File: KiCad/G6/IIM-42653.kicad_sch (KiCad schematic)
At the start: 8 parts, among them U13 IIM-42653, U14 IIM-42653

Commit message: uhhhh im confused gang
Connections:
- net AP-SDI renamed AP-SDI-IIM1
- net AP-SDI-IIM1: no longer U14.14 (AP_SDA/AP_SDIO/AP_SDI)
- net AP-SDO renamed AP-SDO-IIM1
- net AP-SDO-IIM1: no longer U14.1 (AP_SDO/AP_AD0)
- net SPI-SDO-MAIN renamed SPI-SDO-IIM1
- net SPI-SDO-IIM1: no longer U14.11 (AUX1_SDO)
- new net AP-SDI-IIM2: U14.14 (AP_SDA/AP_SDIO/AP_SDI)
- new net AP-SDO-IIM2: U14.1 (AP_SDO/AP_AD0)
- new net SPI-SDO-IIM2: U14.11 (AUX1_SDO)
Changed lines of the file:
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@@
 		)
 	)
-	(global_label "AP-SDI"
+	(global_label "AP-SDI-IIM1"
 		(shape input)
 		(at 44.45 92.71 180)
@@
 		)
 		(property "Intersheetrefs" "${INTERSHEET_REFS}"
-			(at 34.4495 92.71 0)
+			(at 29.0066 92.71 0)
 			(effects
 				(font
@@
 		)
 	)
-	(global_label "AP-SDO"
+	(global_label "AP-SDO-IIM1"
 		(shape input)
 		(at 44.45 95.25 180)
@@
 		)
 		(property "Intersheetrefs" "${INTERSHEET_REFS}"
-			(at 33.7238 95.25 0)
+			(at 28.2809 95.25 0)
 			(effects
 				(font
@@
 		)
 	)
-	(global_label "SPI-SDO-MAIN"
+	(global_label "SPI-SDO-IIM1"
 		(shape input)
 		(at 44.45 107.95 180)
@@
 		)
 		(property "Intersheetrefs" "${INTERSHEET_REFS}"
-			(at 26.9504 107.95 0)
+			(at 27.5552 107.95 0)
 			(effects
 				(font
@@
 		)
 	)
-	(global_label "AP-SDI"
+	(global_label "AP-SDI-IIM2"
 		(shape input)
 		(at 180.34 100.33 180)
@@
 		)
 		(property "Intersheetrefs" "${INTERSHEET_REFS}"
-			(at 170.3395 100.33 0)
+			(at 164.8966 100.33 0)
 			(effects
 				(font
@@
 		)
 	)
-	(global_label "AP-SDO"
+	(global_label "AP-SDO-IIM2"
 		(shape input)
 		(at 180.34 102.87 180)
@@
 		)
 		(property "Intersheetrefs" "${INTERSHEET_REFS}"
-			(at 169.6138 102.87 0)
-			(effects
-				(font
-					(size 1.27 1.27)
-				)
-				(justify right)
-				(hide yes)
-			)
-		)
-	)
-	(global_label "SPI-SDO-MAIN"
+			(at 164.1709 102.87 0)
+			(effects
+				(font
+					(size 1.27 1.27)
+				)
+				(justify right)
+				(hide yes)
+			)
+		)
+	)
+	(global_label "SPI-SDO-IIM2"
 		(shape input)
 		(at 180.34 115.57 180)
@@
 		)
 		(property "Intersheetrefs" "${INTERSHEET_REFS}"
-			(at 162.8404 115.57 0)
-			(effects
-				(font
+			(at 163.4452 115.57 0)
+			(effects
+				(font

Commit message: I think the schematics done uhhh idrk
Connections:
- net AP-CS-IIM1 is gone; now on net CS-IIM1: U13.12 (AP_CS)
- net AP-CS-IIM2 is gone; now on net CS-IIM2: U14.12 (AP_CS)
- net CS-IIM1: no longer U13.10 (AUX1_CS)
- net CS-IIM2: no longer U14.10 (AUX1_CS)
- net AP-SCLK renamed SCK-MAIN
- net AP-SDI-IIM1 renamed MOSI-IIM1
- net AP-SDI-IIM2 renamed MOSI-IIM2
- net AP-SDO-IIM1 renamed MISO-IIM1
- net AP-SDO-IIM2 renamed MISO-IIM2
- net INT1-IIM1-43: no longer names the net of U13.4 (INT1/INT)
- net INT1-IIM2-43: no longer names the net of U14.4 (INT1/INT)
- net INT2-IIM1-43: no longer names the net of U13.9 (INT2/FSYNC/CLKIN)
- net INT2-IIM2-43: no longer names the net of U14.9 (INT2/FSYNC/CLKIN)
- net SPI-SCK-MAIN: no longer names the net of U13.3 (AUX1_SCLK)
- net SPI-SCK-MAIN: no longer U14.3 (AUX1_SCLK)
- net SPI-SDO-IIM1: no longer names the net of U13.11 (AUX1_SDO)
- net SPI-SDO-IIM2: no longer names the net of U14.11 (AUX1_SDO)

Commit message: im sorry parsa :/
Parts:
- U13, U14: footprint IIM-42653:PQFN50P250X300X97-14N -> CC0603KRXQRQBB104:IIM42563
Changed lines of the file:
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@@
 			)
 		)
-		(property "Footprint" "IIM-42653:PQFN50P250X300X97-14N"
+		(property "Footprint" "CC0603KRXQRQBB104:IIM42563"
 			(at 72.39 100.33 0)
 			(effects
@@
 			)
 		)
-		(property "Footprint" "IIM-42653:PQFN50P250X300X97-14N"
+		(property "Footprint" "CC0603KRXQRQBB104:IIM42563"
 			(at 208.28 107.95 0)
 			(effects

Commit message: sasha sneaky academic
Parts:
- renumbered C8 to C10, C9 to C11, C10 to C12, C11 to C13, C6 to C8, C7 to C9, U13 to U10, U14 to U11
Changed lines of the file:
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@@
 		(dnp no)
 		(fields_autoplaced yes)
-		(property "Reference" "C8"
+		(property "Reference" "C10"
 			(at 121.92 86.3599 0)
 			(effects
@@
 			(project ""
 				(path "/99017594-210d-4d15-87a7-3152ef0d7b7c/5c9dde29-c732-426e-b6f2-0733aa54ee5a"
-					(reference "C8")
+					(reference "C10")
 					(unit 1)
 				)
@@
 		(dnp no)
 		(fields_autoplaced yes)
-		(property "Reference" "C6"
+		(property "Reference" "C8"
 			(at 110.49 74.9299 0)
 			(effects
@@
 			(project "G6"
 				(path "/99017594-210d-4d15-87a7-3152ef0d7b7c/5c9dde29-c732-426e-b6f2-0733aa54ee5a"
-					(reference "C6")
+					(reference "C8")
 					(unit 1)
 				)
@@
 		(dnp no)
 		(fields_autoplaced yes)
-		(property "Reference" "#PWR049"
+		(property "Reference" "#PWR042"
 			(at 106.68 66.04 0)
 			(effects
@@
 			(project ""
 				(path "/99017594-210d-4d15-87a7-3152ef0d7b7c/5c9dde29-c732-426e-b6f2-0733aa54ee5a"
-					(reference "#PWR049")
+					(reference "#PWR042")
 					(unit 1)
 				)
@@
 		(dnp no)
 		(fields_autoplaced yes)
-		(property "Reference" "#PWR035"
+		(property "Reference" "#PWR041"
 			(at 102.87 130.81 0)
 			(effects
@@
 			(project ""
 				(path "/99017594-210d-4d15-87a7-3152ef0d7b7c/5c9dde29-c732-426e-b6f2-0733aa54ee5a"
-					(reference "#PWR035")
+					(reference "#PWR041")
 					(unit 1)
 				)
@@
 		(dnp no)
 		(fields_autoplaced yes)
-		(property "Reference" "C10"
+		(property "Reference" "C12"
 			(at 246.38 93.9799 0)
 			(effects
@@
 			(project "G6"
 				(path "/99017594-210d-4d15-87a7-3152ef0d7b7c/5c9dde29-c732-426e-b6f2-0733aa54ee5a"
-					(reference "C10")
+					(reference "C12")
 					(unit 1)
 				)
@@
 		(dnp no)
 		(fields_autoplaced yes)
-		(property "Reference" "C7"
+		(property "Reference" "C9"
 			(at 110.49 86.3599 0)
 			(effects
@@
 			(project "G6"
 				(path "/99017594-210d-4d15-87a7-3152ef0d7b7c/5c9dde29-c732-426e-b6f2-0733aa54ee5a"
-					(reference "C7")
+					(reference "C9")
 					(unit 1)
 				)
@@
 		(dnp no)
 		(fields_autoplaced yes)
-		(property "Reference" "#PWR065"
+		(property "Reference" "#PWR048"
 			(at 254 106.68 0)
 			(effects
@@
 			(project "G6"
 				(path "/99017594-210d-4d15-87a7-3152ef0d7b7c/5c9dde29-c732-426e-b6f2-0733aa54ee5a"
-					(reference "#PWR065")
+					(reference "#PWR048")
 					(unit 1)
 				)
@@
 		(dnp no)
 		(fields_autoplaced yes)
-		(property "Reference" "C9"
+		(property "Reference" "C11"
 			(at 246.38 82.5499 0)
 			(effects
@@
 			(project "G6"
 				(path "/99017594-210d-4d15-87a7-3152ef0d7b7c/5c9dde29-c732-426e-b6f2-0733aa54ee5a"
-					(reference "C9")
+					(reference "C11")
 					(unit 1)
 				)
@@
 		(dnp no)
 		(fields_autoplaced yes)
-		(property "Reference" "U13"
+		(property "Reference" "U10"
 			(at 72.39 72.39 0)
 			(effects
@@
 			(project ""
 				(path "/99017594-210d-4d15-87a7-3152ef0d7b7c/5c9dde29-c732-426e-b6f2-0733aa54ee5a"
-					(reference "U13")
+					(reference "U10")
 					(unit 1)
 				)
@@
 		(dnp no)
 		(fields_autoplaced yes)
-		(property "Reference" "C11"
+		(property "Reference" "C13"
 			(at 257.81 93.9799 0)
 			(effects
@@
 			(project "G6"
 				(path "/99017594-210d-4d15-87a7-3152ef0d7b7c/5c9dde29-c732-426e-b6f2-0733aa54ee5a"
-					(reference "C11")
+					(reference "C13")
 					(unit 1)
 				)
@@
 		(dnp no)
 		(fields_autoplaced yes)
-		(property "Reference" "#PWR061"
+		(property "Reference" "#PWR044"
 			(at 118.11 99.06 0)
 			(effects
@@
 			(project ""
 				(path "/99017594-210d-4d15-87a7-3152ef0d7b7c/5c9dde29-c732-426e-b6f2-0733aa54ee5a"
-					(reference "#PWR061")
+					(reference "#PWR044")
 					(unit 1)
 				)
@@
 		(dnp no)
 		(fields_autoplaced yes)
-		(property "Reference" "#PWR064"
+		(property "Reference" "#PWR047"
 			(at 242.57 105.41 0)
 			(effects
@@
 			(project "G6"
 				(path "/99017594-210d-4d15-87a7-3152ef0d7b7c/5c9dde29-c732-426e-b6f2-0733aa54ee5a"
-					(reference "#PWR064")
+					(reference "#PWR047")
 					(unit 1)
 				)
@@
 		(dnp no)
 		(fields_autoplaced yes)
-		(property "Reference" "#PWR063"
+		(property "Reference" "#PWR046"
 			(at 242.57 73.66 0)
 			(effects
@@
 			(project "G6"
 				(path "/99017594-210d-4d15-87a7-3152ef0d7b7c/5c9dde29-c732-426e-b6f2-0733aa54ee5a"
-					(reference "#PWR063")
+					(reference "#PWR046")
 					(unit 1)
 				)
@@
 		(dnp no)
 		(fields_autoplaced yes)
-		(property "Reference" "#PWR060"
+		(property "Reference" "#PWR043"
 			(at 106.68 97.79 0)
 			(effects
@@
 			(project ""
 				(path "/99017594-210d-4d15-87a7-3152ef0d7b7c/5c9dde29-c732-426e-b6f2-0733aa54ee5a"
-					(reference "#PWR060")
+					(reference "#PWR043")
 					(unit 1)
 				)
@@
 		(dnp no)
 		(fields_autoplaced yes)
-		(property "Reference" "U14"
+		(property "Reference" "U11"
 			(at 208.28 80.01 0)
 			(effects
@@
 			(project "G6"
 				(path "/99017594-210d-4d15-87a7-3152ef0d7b7c/5c9dde29-c732-426e-b6f2-0733aa54ee5a"
-					(reference "U14")
+					(reference "U11")
 					(unit 1)
 				)
@@
 		(dnp no)
 		(fields_autoplaced yes)
-		(property "Reference" "#PWR062"
+		(property "Reference" "#PWR045"
 			(at 238.76 138.43 0)
 			(effects
@@
 			(project "G6"
 				(path "/99017594-210d-4d15-87a7-3152ef0d7b7c/5c9dde29-c732-426e-b6f2-0733aa54ee5a"
-					(reference "#PWR062")
-					(unit 1)
-				)
+					(reference "#PWR045")
+					(unit 1)
+				)

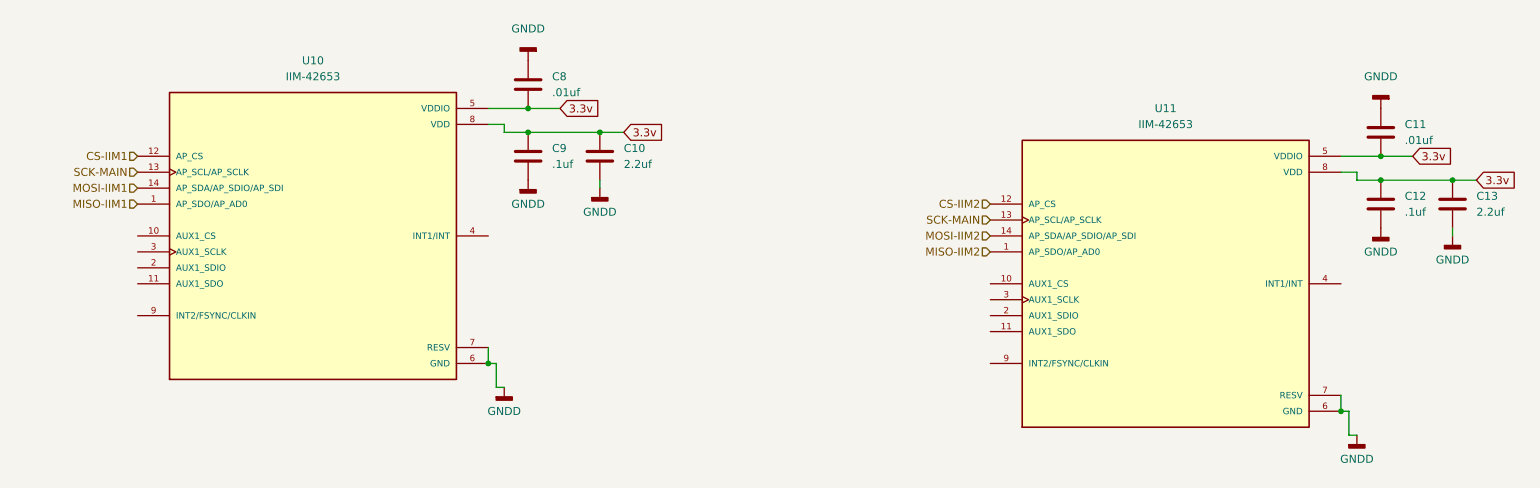
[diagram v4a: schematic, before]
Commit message: errrrrr i cant find a umcx connector they all say there like $50??
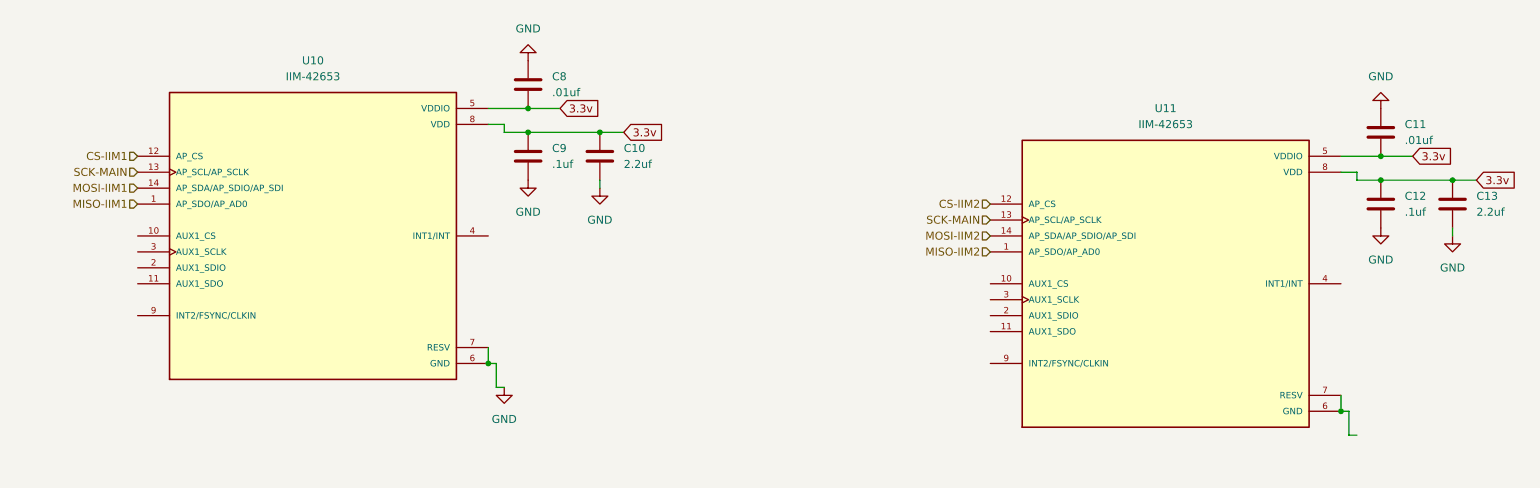
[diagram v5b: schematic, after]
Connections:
- net GNDD renamed GND
- net GND: no longer U11.6 (GND), U11.7 (RESV)
- new net: U11.6 (GND), U11.7 (RESV)

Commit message: i have no idea whats going on, everything crashed and nothing will open
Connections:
- net GND: now also U11.6 (GND), U11.7 (RESV)
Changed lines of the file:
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@@
+	)
+	(symbol
+		(lib_id "power:GND")
+		(at 238.76 132.08 0)
+		(unit 1)
+		(exclude_from_sim no)
+		(in_bom yes)
+		(on_board yes)
+		(dnp no)
+		(fields_autoplaced yes)
+		(property "Reference" "#PWR039"
+			(at 238.76 138.43 0)
+			(effects
+				(font
+					(size 1.27 1.27)
+				)
+				(hide yes)
+			)
+		)
+		(property "Value" "GND"
+			(at 238.76 137.16 0)
+			(effects
+				(font
+					(size 1.27 1.27)
+				)
+			)
+		)
+		(property "Footprint" ""
+			(at 238.76 132.08 0)
+			(effects
+				(font
+					(size 1.27 1.27)
+				)
+				(hide yes)
+			)
+		)
+		(property "Datasheet" ""
+			(at 238.76 132.08 0)
+			(effects
+				(font
+					(size 1.27 1.27)
+				)
+				(hide yes)
+			)
+		)
+		(property "Description" "Power symbol creates a global label with name \"GND\" , ground"
+			(at 238.76 132.08 0)
+			(effects
+				(font
+					(size 1.27 1.27)
+				)
+				(hide yes)
+			)
+		)
+		(pin "1"
+		)
+		(instances
+			(project ""
+				(path "/99017594-210d-4d15-87a7-3152ef0d7b7c/5c9dde29-c732-426e-b6f2-0733aa54ee5a"
+					(reference "#PWR039")
+					(unit 1)
+				)
+			)
+		)
 	)
 	(symbol

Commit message: g6
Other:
- moved on the sheet: C11, C8
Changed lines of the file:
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@@
 	)
 	(junction
-		(at 106.68 80.01)
+		(at 106.68 78.74)
 		(diameter 0)
 		(color 0 0 0 0)
@@
 	)
 	(junction
-		(at 242.57 87.63)
+		(at 242.57 86.36)
 		(diameter 0)
 		(color 0 0 0 0)
@@
 	(wire
 		(pts
-			(xy 237.49 132.08) (xy 237.49 128.27)
-		)
-		(stroke
-			(width 0)
-			(type default)
-		)
-	)
-	(wire
-		(pts
-			(xy 238.76 132.08) (xy 237.49 132.08)
-		)
-		(stroke
-			(width 0)
-			(type default)
-		)
-	)
-	(wire
-		(pts
-			(xy 242.57 87.63) (xy 247.65 87.63)
-		)
-		(stroke
-			(width 0)
-			(type default)
-		)
-	)
-	(wire
-		(pts
-			(xy 101.6 120.65) (xy 100.33 120.65)
-		)
-		(stroke
-			(width 0)
-			(type default)
-		)
-	)
-	(wire
-		(pts
-			(xy 106.68 80.01) (xy 111.76 80.01)
-		)
-		(stroke
-			(width 0)
-			(type default)
-		)
-	)
-	(wire
-		(pts
-			(xy 236.22 87.63) (xy 242.57 87.63)
+			(xy 102.87 80.01) (xy 100.33 80.01)
+		)
+		(stroke
+			(width 0)
+			(type default)
+		)
+	)
+	(wire
+		(pts
+			(xy 238.76 86.36) (xy 238.76 87.63)
+		)
+		(stroke
+			(width 0)
+			(type default)
+		)
+	)
+	(wire
+		(pts
+			(xy 242.57 86.36) (xy 247.65 86.36)
+		)
+		(stroke
+			(width 0)
+			(type default)
+		)
+	)
+	(wire
+		(pts
+			(xy 106.68 78.74) (xy 111.76 78.74)
+		)
+		(stroke
+			(width 0)
+			(type default)
+		)
+	)
+	(wire
+		(pts
+			(xy 238.76 86.36) (xy 242.57 86.36)
 		)
 		(stroke
@@
 	(wire
 		(pts
-			(xy 102.87 124.46) (xy 101.6 124.46)
-		)
-		(stroke
-			(width 0)
-			(type default)
-		)
-	)
-	(wire
-		(pts
-			(xy 237.49 128.27) (xy 236.22 128.27)
+			(xy 102.87 78.74) (xy 102.87 80.01)
+		)
+		(stroke
+			(width 0)
+			(type default)
+		)
+	)
+	(wire
+		(pts
+			(xy 238.76 87.63) (xy 236.22 87.63)
 		)
 		(stroke
@@
 	(wire
 		(pts
-			(xy 101.6 124.46) (xy 101.6 120.65)
-		)
-		(stroke
-			(width 0)
-			(type default)
-		)
-	)
-	(wire
-		(pts
-			(xy 100.33 80.01) (xy 106.68 80.01)
+			(xy 102.87 78.74) (xy 106.68 78.74)
 		)
 		(stroke
@@
 	(global_label "3.3v"
 		(shape input)
-		(at 247.65 87.63 0)
+		(at 247.65 86.36 0)
 		(fields_autoplaced yes)
 		(effects
@@
 		)
 		(property "Intersheetrefs" "${INTERSHEET_REFS}"
-			(at 254.6266 87.63 0)
+			(at 254.6266 86.36 0)
 			(effects
 				(font
@@
 	(global_label "3.3v"
 		(shape input)
-		(at 111.76 80.01 0)
+		(at 111.76 78.74 0)
 		(fields_autoplaced yes)
 		(effects
@@
 		)
 		(property "Intersheetrefs" "${INTERSHEET_REFS}"
-			(at 118.7366 80.01 0)
+			(at 118.7366 78.74 0)
 			(effects
 				(font
@@
 	(symbol
 		(lib_id "Device:C")
-		(at 106.68 76.2 0)
+		(at 106.68 74.93 0)
 		(unit 1)
 		(exclude_from_sim no)
@@
 		(fields_autoplaced yes)
 		(property "Reference" "C8"
-			(at 110.49 74.9299 0)
+			(at 110.49 73.6599 0)
 			(effects
 				(font
@@
 		)
 		(property "Value" ".01uf"
-			(at 110.49 77.4699 0)
+			(at 110.49 76.1999 0)
 			(effects
 				(font
@@
 		)
 		(property "Footprint" "CC0603KRXQRQBB104:.01YAG_CC1206_YAG"
-			(at 107.6452 80.01 0)
+			(at 107.6452 78.74 0)
 			(effects
 				(font
@@
 		)
 		(property "Datasheet" "~"
-			(at 106.68 76.2 0)
+			(at 106.68 74.93 0)
 			(effects
 				(font
@@
 		)
 		(property "Description" "Unpolarized capacitor"
-			(at 106.68 76.2 0)
+			(at 106.68 74.93 0)
 			(effects
 				(font
@@
 	(symbol
 		(lib_id "power:GND")
-		(at 238.76 132.08 0)
+		(at 236.22 128.27 0)
 		(unit 1)
 		(exclude_from_sim no)
@@
 		(fields_autoplaced yes)
 		(property "Reference" "#PWR039"
-			(at 238.76 138.43 0)
+			(at 236.22 134.62 0)
 			(effects
 				(font
@@
 		)
 		(property "Value" "GND"
-			(at 238.76 137.16 0)
+			(at 236.22 133.35 0)
 			(effects
 				(font
@@
 		)
 		(property "Footprint" ""
-			(at 238.76 132.08 0)
+			(at 236.22 128.27 0)
 			(effects
 				(font
@@
 		)
 		(property "Datasheet" ""
-			(at 238.76 132.08 0)
+			(at 236.22 128.27 0)
 			(effects
 				(font
@@
 		)
 		(property "Description" "Power symbol creates a global label with name \"GND\" , ground"
-			(at 238.76 132.08 0)
+			(at 236.22 128.27 0)
 			(effects
 				(font
@@
 	(symbol
 		(lib_id "Device:C")
-		(at 242.57 83.82 0)
+		(at 242.57 82.55 0)
 		(unit 1)
 		(exclude_from_sim no)
@@
 		(fields_autoplaced yes)
 		(property "Reference" "C11"
-			(at 246.38 82.5499 0)
+			(at 246.38 81.2799 0)
 			(effects
 				(font
@@
 		)
 		(property "Value" ".01uf"
-			(at 246.38 85.0899 0)
+			(at 246.38 83.8199 0)
 			(effects
 				(font
@@
 		)
 		(property "Footprint" "CC0603KRXQRQBB104:.01YAG_CC1206_YAG"
-			(at 243.5352 87.63 0)
+			(at 243.5352 86.36 0)
 			(effects
 				(font
@@
 		)
 		(property "Datasheet" "~"
-			(at 242.57 83.82 0)
+			(at 242.57 82.55 0)
 			(effects
 				(font
@@
 		)
 		(property "Description" "Unpolarized capacitor"
-			(at 242.57 83.82 0)
+			(at 242.57 82.55 0)
 			(effects
 				(font
@@
 	(symbol
 		(lib_id "power:GND")
-		(at 242.57 80.01 180)
+		(at 242.57 78.74 180)
 		(unit 1)
 		(exclude_from_sim no)
@@
 		(fields_autoplaced yes)
 		(property "Reference" "#PWR044"
+			(at 242.57 72.39 0)
+			(effects
+				(font
+					(size 1.27 1.27)
+				)
+				(hide yes)
+			)
+		)
+		(property "Value" "GND"
 			(at 242.57 73.66 0)
 			(effects
@@
 					(size 1.27 1.27)
 				)
-				(hide yes)
-			)
-		)
-		(property "Value" "GND"
-			(at 242.57 74.93 0)
-			(effects
-				(font
-					(size 1.27 1.27)
-				)
 			)
 		)
 		(property "Footprint" ""
-			(at 242.57 80.01 0)
+			(at 242.57 78.74 0)
 			(effects
 				(font
@@
 		)
 		(property "Datasheet" ""
-			(at 242.57 80.01 0)
+			(at 242.57 78.74 0)
 			(effects
 				(font
@@
 		)
 		(property "Description" "Power symbol creates a global label with name \"GND\" , ground"
-			(at 242.57 80.01 0)
+			(at 242.57 78.74 0)
 			(effects
 				(font
@@
 	(symbol
 		(lib_id "power:GND")
-		(at 106.68 72.39 180)
+		(at 106.68 71.12 180)
 		(unit 1)
 		(exclude_from_sim no)
@@
 		(fields_autoplaced yes)
 		(property "Reference" "#PWR040"
+			(at 106.68 64.77 0)
+			(effects
+				(font
+					(size 1.27 1.27)
+				)
+				(hide yes)
+			)
+		)
+		(property "Value" "GND"
 			(at 106.68 66.04 0)
 			(effects
@@
 					(size 1.27 1.27)
 				)
-				(hide yes)
-			)
-		)
-		(property "Value" "GND"
-			(at 106.68 67.31 0)
-			(effects
-				(font
-					(size 1.27 1.27)
-				)
 			)
 		)
 		(property "Footprint" ""
-			(at 106.68 72.39 0)
+			(at 106.68 71.12 0)
 			(effects
 				(font
@@
 		)
 		(property "Datasheet" ""
-			(at 106.68 72.39 0)
+			(at 106.68 71.12 0)
 			(effects
 				(font
@@
 		)
 		(property "Description" "Power symbol creates a global label with name \"GND\" , ground"
-			(at 106.68 72.39 0)
+			(at 106.68 71.12 0)
 			(effects
 				(font
@@
 	(symbol
 		(lib_id "power:GND")
-		(at 102.87 124.46 0)
+		(at 100.33 120.65 0)
 		(unit 1)
 		(exclude_from_sim no)
@@
 		(fields_autoplaced yes)
 		(property "Reference" "#PWR043"
-			(at 102.87 130.81 0)
+			(at 100.33 127 0)
 			(effects
 				(font
@@
 		)
 		(property "Value" "GND"
-			(at 102.87 129.54 0)
+			(at 100.33 125.73 0)
 			(effects
 				(font
@@
 		)
 		(property "Footprint" ""
-			(at 102.87 124.46 0)
+			(at 100.33 120.65 0)
 			(effects
 				(font
@@
 		)
 		(property "Datasheet" ""
-			(at 102.87 124.46 0)
+			(at 100.33 120.65 0)
 			(effects
 				(font
@@
 		)
 		(property "Description" "Power symbol creates a global label with name \"GND\" , ground"
-			(at 102.87 124.46 0)
-			(effects
-				(font
+			(at 100.33 120.65 0)
+			(effects
+				(font
